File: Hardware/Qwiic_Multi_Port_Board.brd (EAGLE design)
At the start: 25.4 x 25.4 mm, 16 parts, among them J1 QWIIC_RIGHT_ANGLE, J2 QWIIC_RIGHT_ANGLE, J3 QWIIC_RIGHT_ANGLE, J4 QWIIC_RIGHT_ANGLE

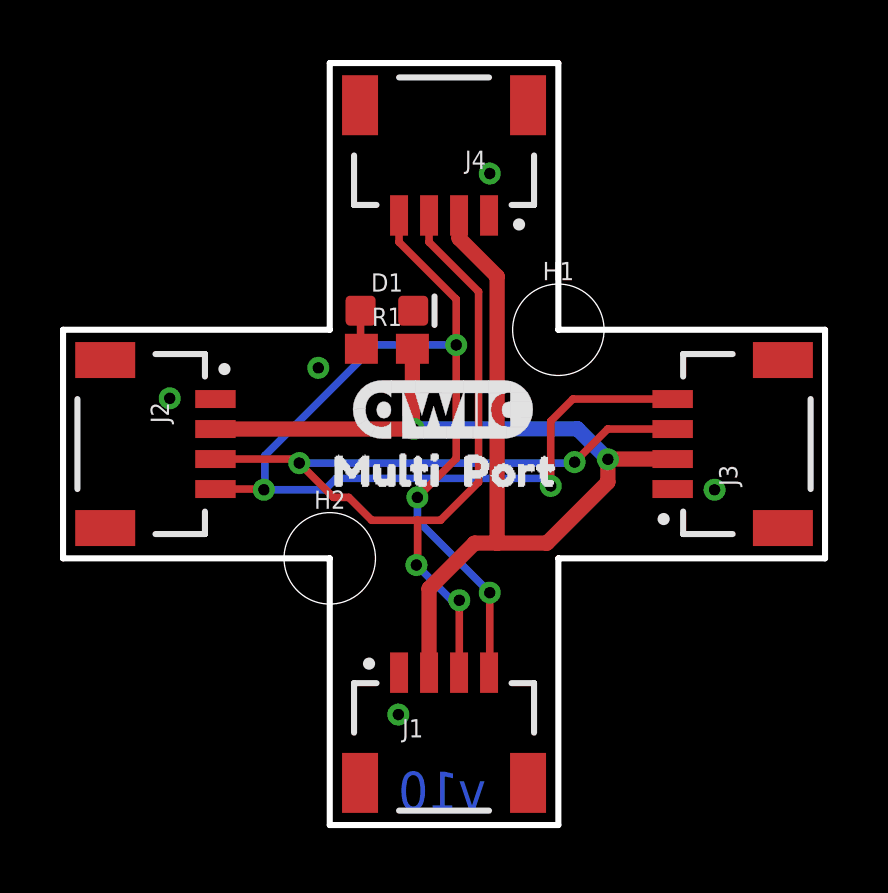
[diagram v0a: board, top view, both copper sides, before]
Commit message: Update SFE logos on board
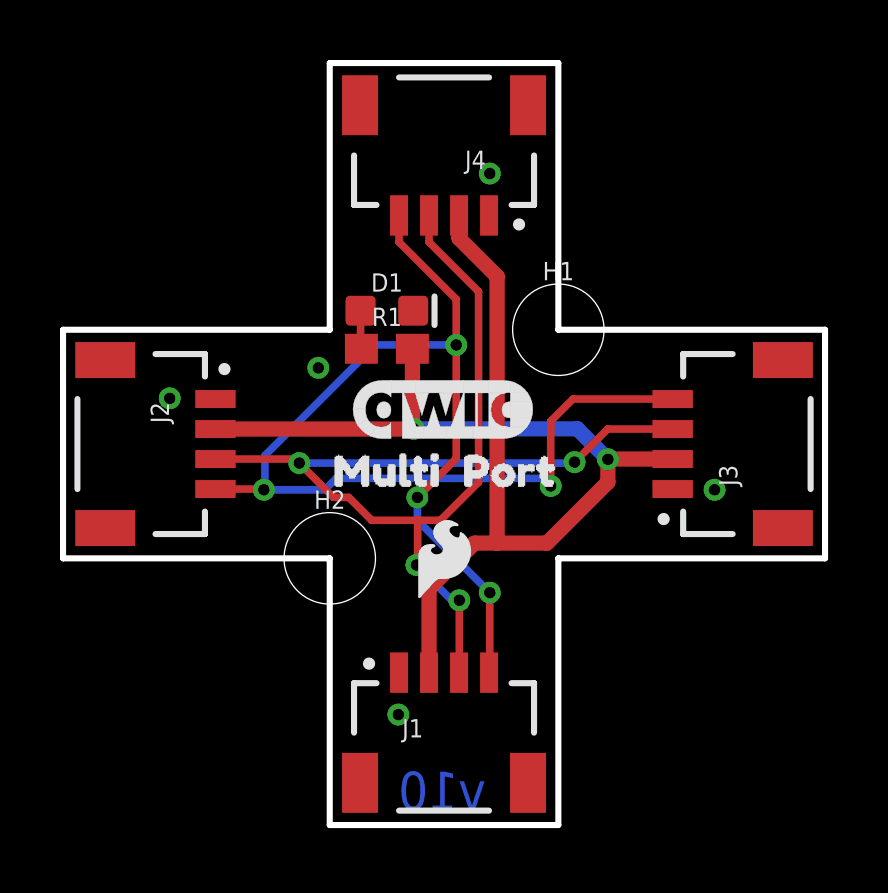
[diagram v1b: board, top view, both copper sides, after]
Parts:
- added U$6: (no value), SparkFun-Aesthetics:SFE_LOGO_NAME_.2
- U$2: device SparkX:SPARKX-SMALL -> SparkFun-Aesthetics:SFE_LOGO_FLAME_.1
- moved U$2 3.30 mm to (12.7, 8.89), flipped to the top
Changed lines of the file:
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@@
 <attribute name="VALUE" x="14.351" y="23.622" size="0.6096" layer="27" font="vector" ratio="20" rot="R180"/>
 </element>
-<element name="U$2" library="SparkX" package="SPARKX-SMALL" value="" x="12.7" y="5.588" smashed="yes" rot="MR0"/>
 <element name="U$4" library="buzzard_labels (75)" package="MULTI1" value="" x="8.128" y="11.811" smashed="yes"/>
 <element name="U$5" library="buzzard_labels (75)" package="PORT2" value="" x="12.446" y="11.811" smashed="yes"/>
@@
 <attribute name="VALUE" x="10.795" y="15.113" size="0.6096" layer="27" font="vector" ratio="20" align="top-center"/>
 </element>
+<element name="U$2" library="SparkFun-Aesthetics" package="SFE_LOGO_FLAME_.1" value="" x="12.7" y="8.89" smashed="yes"/>
+<element name="U$6" library="SparkFun-Aesthetics" package="SFE_LOGO_NAME_.2" value="" x="12.7" y="12.7" smashed="yes" rot="MR0"/>
 </elements>
 <signals>

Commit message: Update silk screen
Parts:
- moved U$8 8.98 mm to (14.2, 2.92)
- moved U$7 8.03 mm to (14.9, 4.19)
- moved U$3 7.62 mm to (12.7, 6.22)
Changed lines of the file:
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@@
 <element name="U$5" library="buzzard_labels (75)" package="PORT2" value="" x="12.446" y="11.811" smashed="yes"/>
 <element name="U$1" library="SparkFun-Aesthetics" package="QWIIC_6MM" value="" x="12.7" y="13.843" smashed="yes"/>
-<element name="U$3" library="SparkFun-Aesthetics" package="QWIIC_6MM" value="" x="12.7" y="13.843" smashed="yes" rot="MR0"/>
-<element name="U$7" library="buzzard_labels (75)" package="MULTI1" value="" x="17.399" y="11.811" smashed="yes" rot="MR0"/>
-<element name="U$8" library="buzzard_labels (75)" package="PORT2" value="" x="12.954" y="11.811" smashed="yes" rot="MR0"/>
+<element name="U$3" library="SparkFun-Aesthetics" package="QWIIC_6MM" value="" x="12.7" y="6.223" smashed="yes" rot="MR0"/>
+<element name="U$7" library="buzzard_labels (75)" package="MULTI1" value="" x="14.859" y="4.191" smashed="yes" rot="MR0"/>
+<element name="U$8" library="buzzard_labels (75)" package="PORT2" value="" x="14.224" y="2.921" smashed="yes" rot="MR0"/>
 <element name="H1" library="SparkFun-Hardware" package="STAND-OFF-TIGHT" value="STAND-OFFTIGHT" x="16.51" y="16.51" smashed="yes">
 <attribute name="NAME" x="16.51" y="18.161" size="0.6096" layer="25" font="vector" ratio="20" align="bottom-center"/>

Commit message: Update silkscreen
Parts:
- removed U$4, U$7: (no value), buzzard_labels (75):MULTI1
- removed U$5, U$8: (no value), buzzard_labels (75):PORT2
- added U$10, U$11: (no value), output:MULTI0
- added U$12, U$13: (no value), output:PORT0
- added U$9: (no value), output:PWR0
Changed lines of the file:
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@@
 <?xml version="1.0" encoding="utf-8"?>
 <!DOCTYPE eagle SYSTEM "eagle.dtd">
-<eagle version="9.5.2">
+<eagle version="9.6.2">
 <drawing>
 <settings>
-<setting alwaysvectorfont="yes"/>
+<setting alwaysvectorfont="no"/>
 <setting verticaltext="up"/>
 </settings>
@@
 <attribute name="VALUE" x="14.351" y="23.622" size="0.6096" layer="27" font="vector" ratio="20" rot="R180"/>
 </element>
-<element name="U$4" library="buzzard_labels (75)" package="MULTI1" value="" x="8.128" y="11.811" smashed="yes"/>
-<element name="U$5" library="buzzard_labels (75)" package="PORT2" value="" x="12.446" y="11.811" smashed="yes"/>
 <element name="U$1" library="SparkFun-Aesthetics" package="QWIIC_6MM" value="" x="12.7" y="13.843" smashed="yes"/>
 <element name="U$3" library="SparkFun-Aesthetics" package="QWIIC_6MM" value="" x="12.7" y="6.223" smashed="yes" rot="MR0"/>
-<element name="U$7" library="buzzard_labels (75)" package="MULTI1" value="" x="14.859" y="4.191" smashed="yes" rot="MR0"/>
-<element name="U$8" library="buzzard_labels (75)" package="PORT2" value="" x="14.224" y="2.921" smashed="yes" rot="MR0"/>
 <element name="H1" library="SparkFun-Hardware" package="STAND-OFF-TIGHT" value="STAND-OFFTIGHT" x="16.51" y="16.51" smashed="yes">
 <attribute name="NAME" x="16.51" y="18.161" size="0.6096" layer="25" font="vector" ratio="20" align="bottom-center"/>
@@
 <element name="U$2" library="SparkFun-Aesthetics" package="SFE_LOGO_FLAME_.1" value="" x="12.7" y="8.89" smashed="yes"/>
 <element name="U$6" library="SparkFun-Aesthetics" package="SFE_LOGO_NAME_.2" value="" x="12.7" y="12.7" smashed="yes" rot="MR0"/>
+<element name="U$9" library="output" package="PWR0" value="" x="8.636" y="18.542" smashed="yes"/>
+<element name="U$10" library="output" package="MULTI0" value="" x="8.255" y="11.43" smashed="yes"/>
+<element name="U$11" library="output" package="MULTI0" value="" x="15.24" y="4.191" smashed="yes" rot="MR0"/>
+<element name="U$12" library="output" package="PORT0" value="" x="12.7" y="11.43" smashed="yes"/>
+<element name="U$13" library="output" package="PORT0" value="" x="14.986" y="2.794" smashed="yes" rot="MR0"/>
 </elements>
 <signals>

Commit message: DRC
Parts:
- moved R1 0.25 mm to (10.8, 15.6)

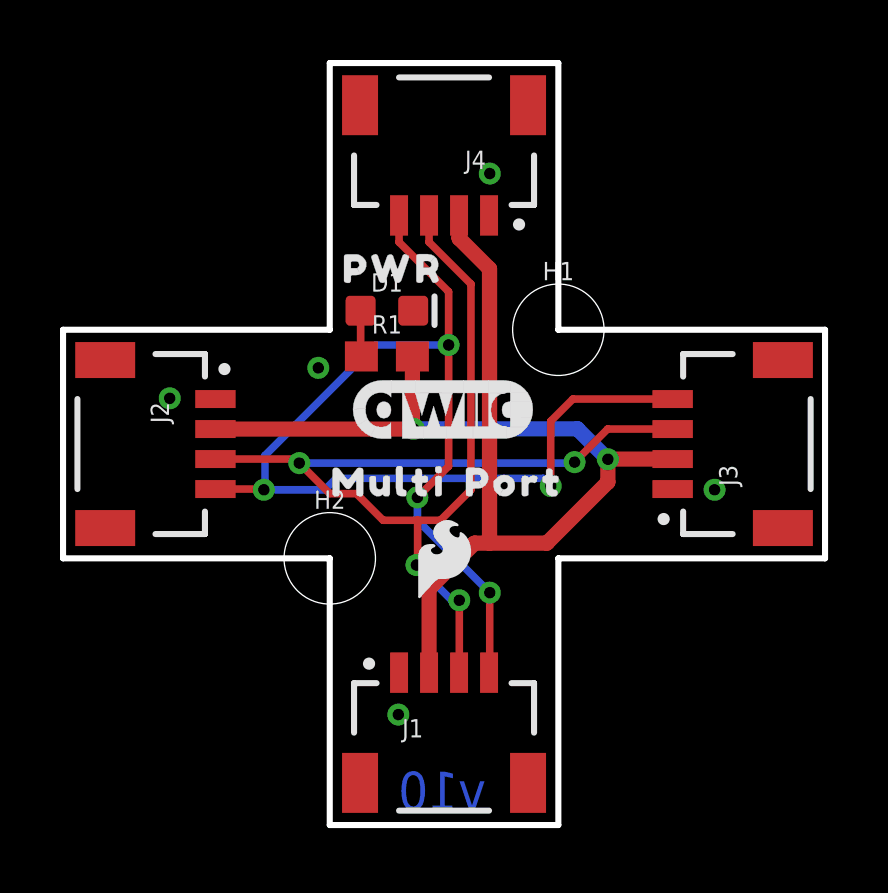
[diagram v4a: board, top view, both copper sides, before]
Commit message: Multi Port: Design Review Changes
Added jumper on PWR LED
Added fiducials
Added OSHW, qwiic, SF logo as device on the schematic
Moved traces on top layer to avoid screws
Decided against:
un-populated I2C pullups -- not enough space
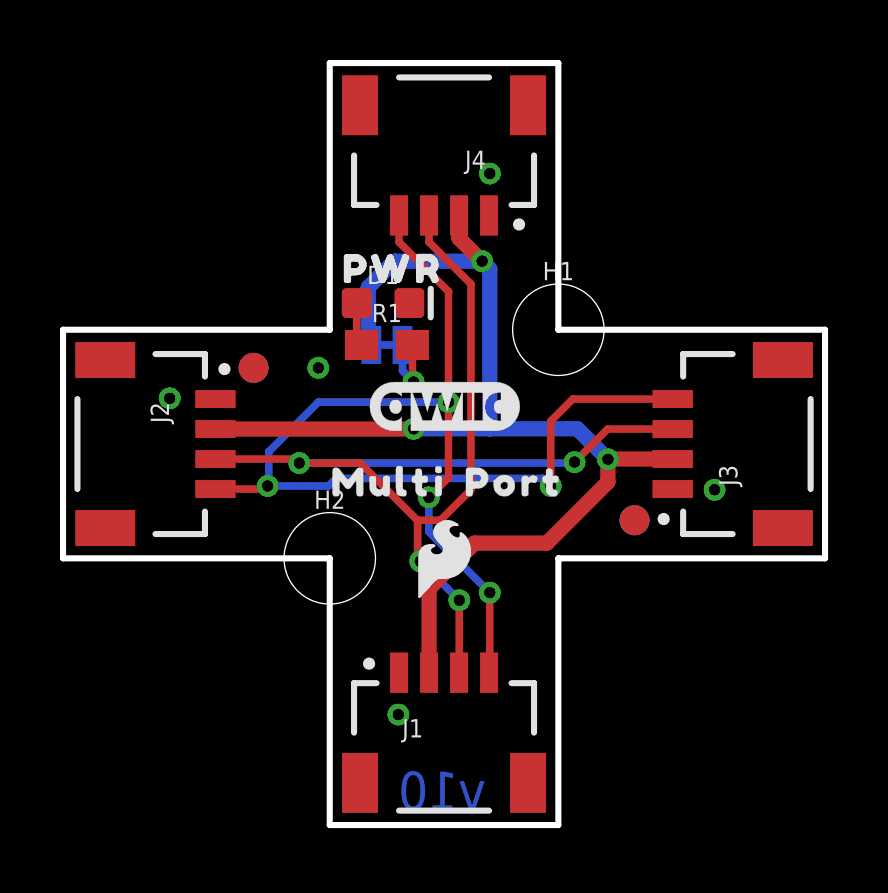
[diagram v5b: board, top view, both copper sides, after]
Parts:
- added FD1, FD2, FD3, FD4: FIDUCIAL1X2, SparkFun-Aesthetics:FIDUCIAL-1X2
- added JP1: PWR_LED, SparkFun-Jumpers:SMT-JUMPER_2_NC_TRACE_SILK
- added LOGO1, LOGO2: QWIIC_LOGO_5MM, SparkFun-Aesthetics:QWIIC_5MM
- added LOGO3: OSHW-LOGOS, SparkFun-Aesthetics:OSHW-LOGO-S
- LOGO4: value (none) -> SFE_LOGO_NAME.2_INCH
- U$1, U$3: device SparkFun-Aesthetics:QWIIC_6MM -> output:PWR0
- moved U$3 11.6 mm to (13.0, 17.8)
- moved U$1 6.21 mm to (8.64, 18.5)
- moved R1 0.38 mm to (10.8, 16.0)
- moved D1 0.28 mm to (10.7, 17.4)
- renumbered U$6 to LOGO4
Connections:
- new net N$2: JP1.1, R1.2
- net 3.3V: now also JP1.2; no longer R1.2
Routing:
- net N$2: track 0.00 -> 2.63 mm, vias 0 -> 1
- net SCL: track 44.1 -> 42.8 mm
- net 3.3V: track 40.4 -> 40.3 mm, vias 2 -> 3

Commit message: Completed Engineering checklist
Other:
- board text added: "in"
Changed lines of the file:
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@@
 <drawing>
 <settings>
-<setting alwaysvectorfont="yes"/>
+<setting alwaysvectorfont="no"/>
 <setting verticaltext="up"/>
 </settings>
@@
 <layer number="37" name="tTest" color="7" fill="1" visible="no" active="yes"/>
 <layer number="38" name="bTest" color="7" fill="1" visible="no" active="yes"/>
-<layer number="39" name="tKeepout" color="4" fill="11" visible="yes" active="yes"/>
+<layer number="39" name="tKeepout" color="4" fill="11" visible="no" active="yes"/>
 <layer number="40" name="bKeepout" color="1" fill="11" visible="no" active="yes"/>
-<layer number="41" name="tRestrict" color="4" fill="10" visible="yes" active="yes"/>
+<layer number="41" name="tRestrict" color="4" fill="10" visible="no" active="yes"/>
 <layer number="42" name="bRestrict" color="1" fill="10" visible="no" active="yes"/>
 <layer number="43" name="vRestrict" color="2" fill="10" visible="no" active="yes"/>
@@
 <layer number="45" name="Holes" color="7" fill="1" visible="yes" active="yes"/>
 <layer number="46" name="Milling" color="3" fill="1" visible="no" active="yes"/>
-<layer number="47" name="Measures" color="7" fill="1" visible="no" active="yes"/>
+<layer number="47" name="Measures" color="7" fill="1" visible="yes" active="yes"/>
 <layer number="48" name="Document" color="7" fill="1" visible="no" active="yes"/>
 <layer number="49" name="Reference" color="7" fill="1" visible="no" active="yes"/>
@@
 <text x="14.097" y="0.508" size="1.27" layer="16" font="vector" ratio="15" rot="MR0">v10</text>
 <text x="48.26" y="-8.89" size="1.27" layer="51" font="vector" ratio="15">Priyanka Makin</text>
+<dimension x1="8.89" y1="25.4" x2="16.51" y2="25.4" x3="12.7" y3="27.94" textsize="1.778" textratio="15" layer="47" unit="inch"/>
+<dimension x1="0" y1="16.51" x2="25.4" y2="16.51" x3="12.7" y3="33.02" textsize="1.778" textratio="15" layer="47" unit="inch"/>
+<text x="16.002" y="33.782" size="1.778" layer="47" font="vector" ratio="15">in</text>
+<text x="17.399" y="28.575" size="1.778" layer="47" font="vector" ratio="15">in</text>
 </plain>
 <attributes>
@@
 <contactref element="J4" pad="2"/>
 <via x="11.684" y="13.208" extent="1-16" drill="0.381"/>
-<wire x1="17.145" y1="13.208" x2="14.224" y2="13.208" width="0.508" layer="16"/>
-<wire x1="14.224" y1="13.208" x2="11.684" y2="13.208" width="0.508" layer="16"/>
+<wire x1="17.145" y1="13.208" x2="13.716" y2="13.208" width="0.508" layer="16"/>
+<wire x1="13.716" y1="13.208" x2="11.684" y2="13.208" width="0.508" layer="16"/>
 <wire x1="17.145" y1="13.208" x2="18.161" y2="12.192" width="0.508" layer="16"/>
 <via x="18.161" y="12.192" extent="1-16" drill="0.381"/>
@@
 <wire x1="13.962" y1="18.796" x2="13.97" y2="18.796" width="0.508" layer="1"/>
 <via x="13.97" y="18.796" extent="1-16" drill="0.381"/>
-<wire x1="13.97" y1="18.796" x2="14.224" y2="18.542" width="0.508" layer="16"/>
-<wire x1="14.224" y1="18.542" x2="14.224" y2="13.208" width="0.508" layer="16"/>
 <wire x1="13.97" y1="18.796" x2="11.049" y2="18.796" width="0.508" layer="16"/>
-<wire x1="10.1727" y1="17.9197" x2="10.1727" y2="16.002" width="0.508" layer="16"/>
-<wire x1="11.049" y1="18.796" x2="10.1727" y2="17.9197" width="0.508" layer="16"/>
-<wire x1="10.1727" y1="16.002" x2="10.2743" y2="16.002" width="0" layer="19" extent="16-16"/>
+<wire x1="11.049" y1="18.796" x2="10.3505" y2="18.0975" width="0.508" layer="16"/>
+<wire x1="13.97" y1="18.796" x2="13.97" y2="18.288" width="0.508" layer="16"/>
+<wire x1="13.97" y1="18.288" x2="13.208" y2="17.526" width="0.508" layer="16"/>
+<wire x1="13.208" y1="14.986" x2="13.716" y2="14.478" width="0.508" layer="16"/>
+<wire x1="13.716" y1="14.478" x2="13.716" y2="13.208" width="0.508" layer="16"/>
+<wire x1="13.208" y1="17.526" x2="13.208" y2="14.986" width="0.508" layer="16"/>
+<wire x1="10.2743" y1="16.002" x2="10.2743" y2="18.0213" width="0.508" layer="16"/>
+<wire x1="10.2743" y1="18.0213" x2="10.3505" y2="18.0975" width="0.508" layer="16"/>
 </signal>
 <signal name="N$1">
 <contactref element="D1" pad="A"/>
 <contactref element="R1" pad="1"/>
-<wire x1="9.791" y1="16.156" x2="9.945" y2="16.002" width="0.254" layer="1"/>
-<wire x1="9.791" y1="17.399" x2="9.791" y2="16.156" width="0.254" layer="1"/>
+<wire x1="9.791" y1="17.399" x2="9.945" y2="17.245" width="0.254" layer="1"/>
+<wire x1="9.945" y1="17.245" x2="9.945" y2="16.002" width="0.254" layer="1"/>
 </signal>
 <signal name="N$2">
